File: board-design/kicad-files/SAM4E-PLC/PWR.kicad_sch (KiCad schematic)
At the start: 21 parts, among them Q1 BC817, U14 LM2576HVS-3.3

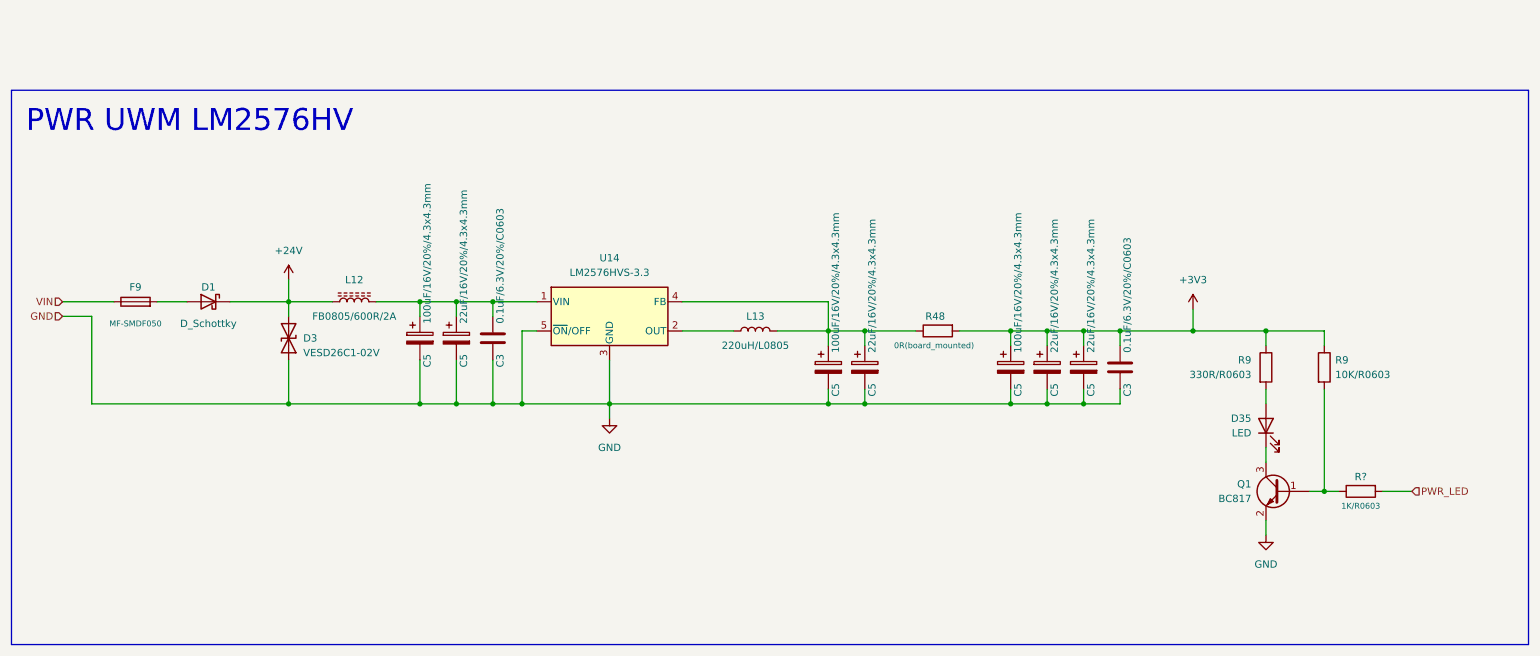
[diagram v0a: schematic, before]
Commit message: [UPDATE]
Refactored schematic for LTE, Power and other schematic sub-sheets.

Signed-off-by: Nicolae-Andrei Vasile <vasilenicolaeandrei@gmail.com>
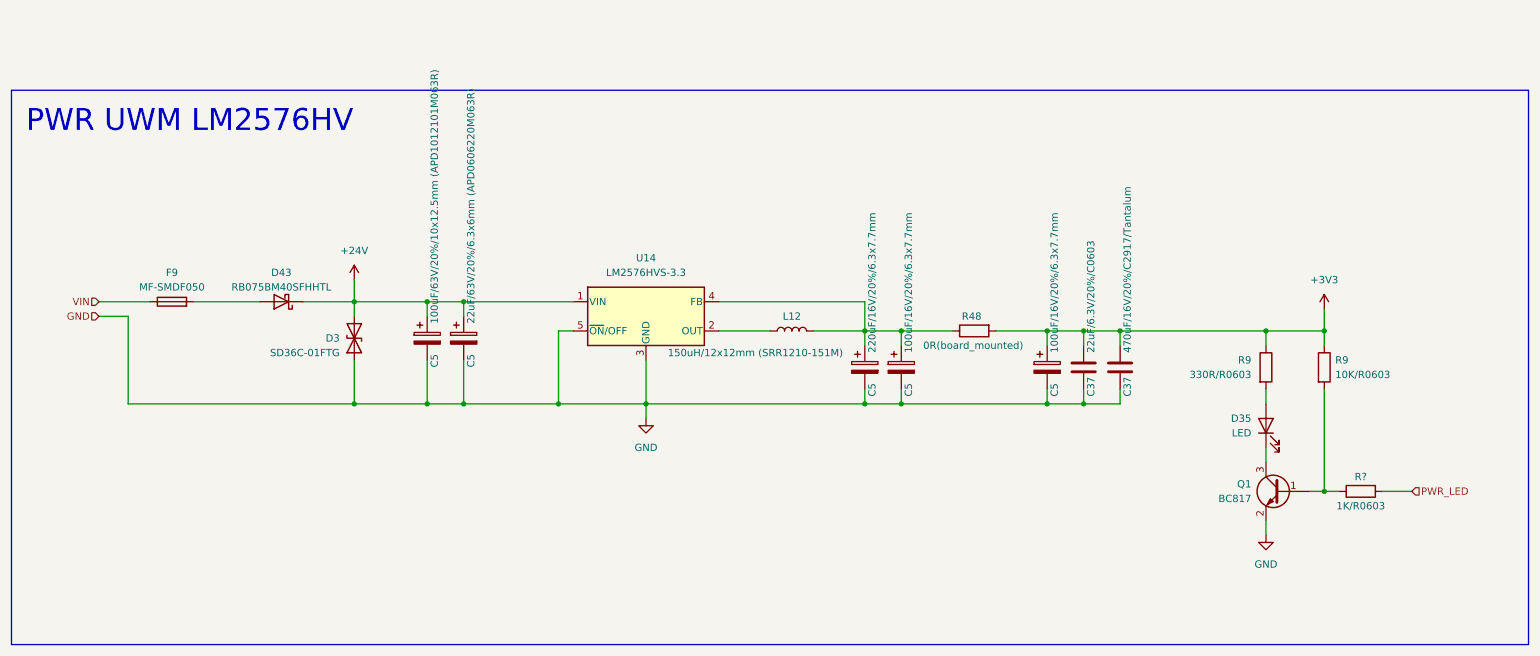
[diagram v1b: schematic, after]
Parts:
- removed C3 (x2): 0.1uF/6.3V/20%/C0603, symbol Device:C
- removed C5 (x2): 22uF/16V/20%/4.3x4.3mm, symbol Device:C_Polarized
- removed C5: 100uF/16V/20%/4.3x4.3mm, symbol Device:C_Polarized
- removed D1: D_Schottky, symbol SparkFun-DiscreteSemi:D_Schottky
- removed L12: FB0805/600R/2A, symbol Device:L_Ferrite
- added C37: 470uF/16V/20%/C2917/Tantalum, Capacitor_Tantalum_SMD:CP_EIA-7343-30_AVX-N, symbol Device:C
- added C37: 22uF/6.3V/20%/C0603, symbol Device:C
- added C5: 100uF/16V/20%/6.3x7.7mm, Capacitor_SMD:CP_Elec_6.3x7.7, symbol Device:C_Polarized
- added D43: RB075BM40SFHHTL, digikey-footprints:TO-252-3, symbol Device:D_Schottky
- C5: value 22uF/16V/20%/4.3x4.3mm -> 22uF/63V/20%/6.3x6mm (APD0606220M063R); footprint (none) -> Capacitor_SMD:CP_Elec_6.3x5.9
- C5: value 100uF/16V/20%/4.3x4.3mm -> 220uF/16V/20%/6.3x7.7mm; footprint (none) -> Capacitor_SMD:CP_Elec_6.3x7.7
- C5: value 100uF/16V/20%/4.3x4.3mm -> 100uF/63V/20%/10x12.5mm (APD1012101M063R); footprint (none) -> Capacitor_SMD:CP_Elec_10x12.5
- C5: value 22uF/16V/20%/4.3x4.3mm -> 100uF/16V/20%/6.3x7.7mm; footprint (none) -> Capacitor_SMD:CP_Elec_6.3x7.7
- D3: value VESD26C1-02V -> SD36C-01FTG; footprint Diode_SMD:D_SOD-523 -> Diode_SMD:D_SOD-323
- D35: footprint (none) -> LED_SMD:LED_0805_2012Metric
- F9: footprint (none) -> Fuse:Fuse_2010_5025Metric
- L12: renamed from L13; value 220uH/L0805 -> 150uH/12x12mm (SRR1210-151M); footprint (none) -> Inductor_SMD:L_12x12mm_H8mm
- R48: footprint (none) -> Resistor_SMD:R_0402_1005Metric
- R9: footprint (none) -> Resistor_SMD:R_0603_1608Metric
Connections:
- net +24V: now also C5.1, C5.1, U14.1 (VIN), D43.1 (K)
- net +3V3: now also C37.1, C37.1, C5.1
- net GND: now also C37.2, C37.2, C5.2
- net at F9.2: now also D43.2 (A)
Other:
- moved on the sheet: C5, D3, F9, L12, R48, U14

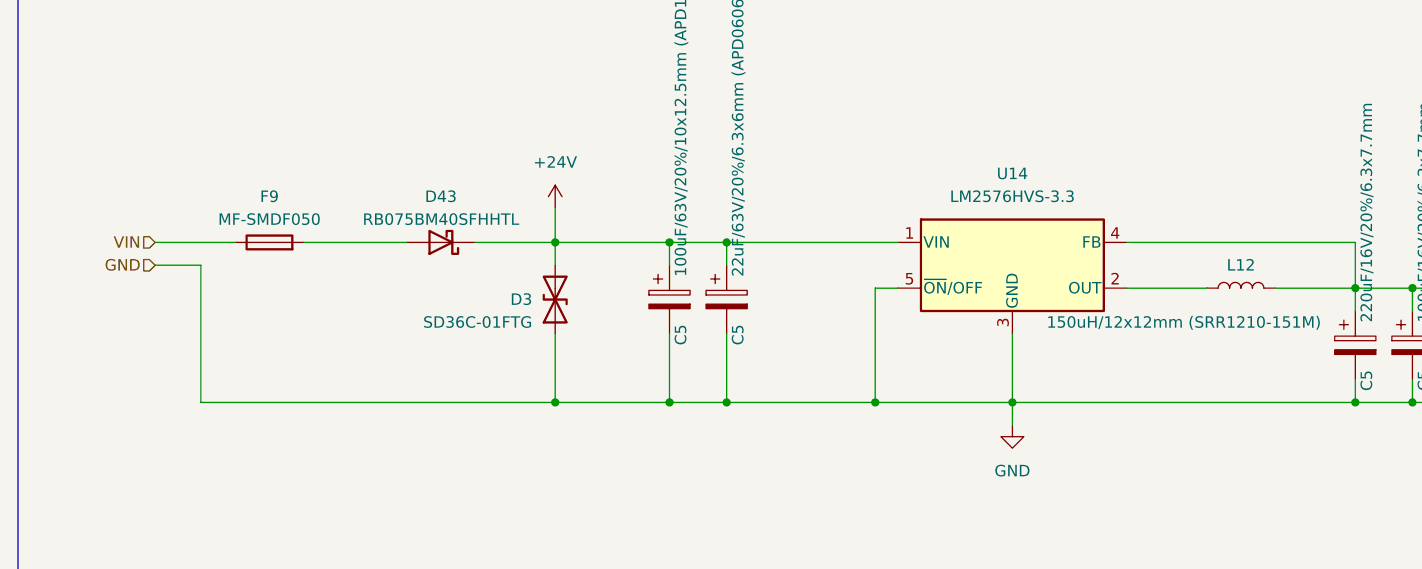
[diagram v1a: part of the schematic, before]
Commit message: [UPDATE]
First draft of SAM4E-PLC schematic completed.

Signed-off-by: Nicolae-Andrei Vasile <vasilenicolaeandrei@gmail.com>
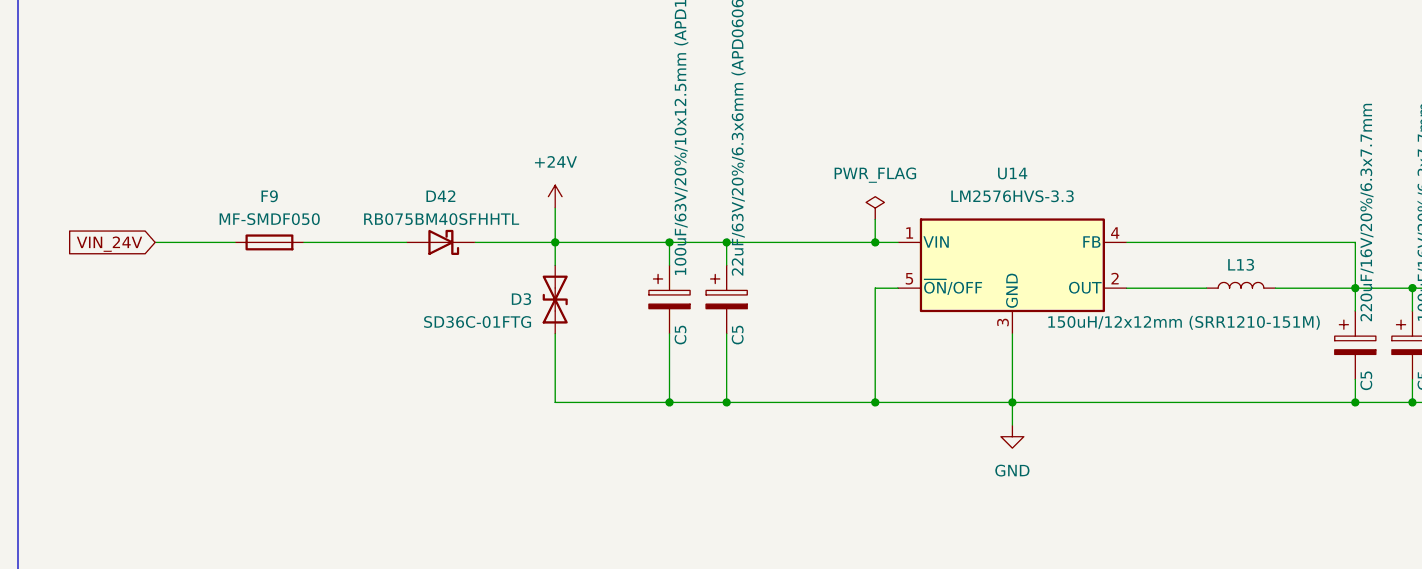
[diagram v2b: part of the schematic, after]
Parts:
- renumbered D43 to D42, L12 to L13
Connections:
- net VIN renamed VIN_24V
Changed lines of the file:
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@@
   (junction (at 196.85 97.79) (diameter 0) (color 0 0 0 0)
   )
+  (junction (at 111.76 92.71) (diameter 0) (color 0 0 0 0)
+  )
   (junction (at 95.25 92.71) (diameter 0) (color 0 0 0 0)
   )
@@
   (junction (at 171.45 110.49) (diameter 0) (color 0 0 0 0)
   )
-  (junction (at 76.2 110.49) (diameter 0) (color 0 0 0 0)
-  )
   (junction (at 95.25 110.49) (diameter 0) (color 0 0 0 0)
   )
@@
     (stroke (width 0) (type default))
   )
-  (wire (pts (xy 36.83 110.49) (xy 76.2 110.49))
-    (stroke (width 0) (type default))
-  )
   (wire (pts (xy 165.1 110.49) (xy 127 110.49))
     (stroke (width 0) (type default))
   )
-  (wire (pts (xy 95.25 92.71) (xy 114.3 92.71))
-    (stroke (width 0) (type default))
-  )
-  (wire (pts (xy 31.75 95.25) (xy 36.83 95.25))
+  (wire (pts (xy 95.25 92.71) (xy 111.76 92.71))
     (stroke (width 0) (type default))
   )
@@
     (stroke (width 0) (type default))
   )
-  (wire (pts (xy 36.83 110.49) (xy 36.83 95.25))
-    (stroke (width 0) (type default))
-  )
   (wire (pts (xy 245.11 125.73) (xy 242.57 125.73))
     (stroke (width 0) (type default))
@@
     (stroke (width 0) (type default))
   )
+  (wire (pts (xy 111.76 90.17) (xy 111.76 92.71))
+    (stroke (width 0) (type default))
+  )
   (wire (pts (xy 88.9 110.49) (xy 95.25 110.49))
     (stroke (width 0) (type default))
@@
   )
   (wire (pts (xy 76.2 92.71) (xy 76.2 95.25))
+    (stroke (width 0) (type default))
+  )
+  (wire (pts (xy 111.76 92.71) (xy 114.3 92.71))
     (stroke (width 0) (type default))
   )
@@
     (effects (font (size 3.81 3.81) (color 140 140 0 1)) (justify left bottom))
   )
+  (global_label "VIN_24V" (shape input) (at 31.75 92.71 180) (fields_autoplaced)
+    (effects (font (size 1.27 1.27)) (justify right))
+    (property "Intersheetrefs" "${INTERSHEET_REFS}" (at 21.2657 92.71 0)
+      (effects (font (size 1.27 1.27)) (justify right) hide)
+    )
+  )
   (hierarchical_label "PWR_LED" (shape input) (at 260.35 125.73 0) (fields_autoplaced)
     (effects (font (size 1.27 1.27)) (justify left))
   )
-  (hierarchical_label "VIN" (shape input) (at 31.75 92.71 180) (fields_autoplaced)
-    (effects (font (size 1.27 1.27)) (justify right))
-  )
-  (hierarchical_label "GND" (shape input) (at 31.75 95.25 180) (fields_autoplaced)
-    (effects (font (size 1.27 1.27)) (justify right))
-  )
   (symbol (lib_id "Device:C_Polarized") (at 196.85 104.14 0) (unit 1)
     (in_bom yes) (on_board yes) (dnp no)
@@
         )
         (path "/93076d8a-73da-4f5d-b7f2-28678f1db77d/aee81a7b-cba1-4b89-a883-459d3f783e91"
-          (reference "C69") (unit 1)
+          (reference "C92") (unit 1)
         )
       )
@@
         )
         (path "/93076d8a-73da-4f5d-b7f2-28678f1db77d/aee81a7b-cba1-4b89-a883-459d3f783e91"
-          (reference "C66") (unit 1)
+          (reference "C89") (unit 1)
         )
       )
@@
         )
         (path "/93076d8a-73da-4f5d-b7f2-28678f1db77d/aee81a7b-cba1-4b89-a883-459d3f783e91"
-          (reference "C71") (unit 1)
+          (reference "C94") (unit 1)
         )
       )
@@
   (symbol (lib_id "power:GND") (at 234.95 133.35 0) (unit 1)
     (in_bom yes) (on_board yes) (dnp no) (fields_autoplaced)
-    (property "Reference" "#PWR072" (at 234.95 139.7 0)
+    (property "Reference" "#PWR085" (at 234.95 139.7 0)
       (effects (font (size 1.27 1.27)) hide)
     )
@@
       (project "SAM4E-PLC"
         (path "/93076d8a-73da-4f5d-b7f2-28678f1db77d/aee81a7b-cba1-4b89-a883-459d3f783e91"
-          (reference "#PWR072") (unit 1)
+          (reference "#PWR085") (unit 1)
         )
       )
@@
   (symbol (lib_id "power:+3V3") (at 245.11 93.98 0) (unit 1)
     (in_bom yes) (on_board yes) (dnp no) (fields_autoplaced)
-    (property "Reference" "#PWR073" (at 245.11 97.79 0)
+    (property "Reference" "#PWR086" (at 245.11 97.79 0)
       (effects (font (size 1.27 1.27)) hide)
     )
@@
       (project "SAM4E-PLC"
         (path "/93076d8a-73da-4f5d-b7f2-28678f1db77d/aee81a7b-cba1-4b89-a883-459d3f783e91"
-          (reference "#PWR073") (unit 1)
+          (reference "#PWR086") (unit 1)
         )
       )
@@
         )
         (path "/93076d8a-73da-4f5d-b7f2-28678f1db77d/aee81a7b-cba1-4b89-a883-459d3f783e91"
-          (reference "C67") (unit 1)
+          (reference "C90") (unit 1)
         )
       )
@@
         )
         (path "/93076d8a-73da-4f5d-b7f2-28678f1db77d/aee81a7b-cba1-4b89-a883-459d3f783e91"
-          (reference "D44") (unit 1)
+          (reference "D43") (unit 1)
         )
       )
@@
   (symbol (lib_id "power:+24V") (at 76.2 88.9 0) (unit 1)
     (in_bom yes) (on_board yes) (dnp no) (fields_autoplaced)
-    (property "Reference" "#PWR070" (at 76.2 92.71 0)
+    (property "Reference" "#PWR083" (at 76.2 92.71 0)
       (effects (font (size 1.27 1.27)) hide)
     )
@@
       (project "SAM4E-PLC"
         (path "/93076d8a-73da-4f5d-b7f2-28678f1db77d/aee81a7b-cba1-4b89-a883-459d3f783e91"
-          (reference "#PWR070") (unit 1)
+          (reference "#PWR083") (unit 1)
         )
       )
@@
   (symbol (lib_id "power:GND") (at 127 113.03 0) (unit 1)
     (in_bom yes) (on_board yes) (dnp no) (fields_autoplaced)
-    (property "Reference" "#PWR071" (at 127 119.38 0)
+    (property "Reference" "#PWR084" (at 127 119.38 0)
       (effects (font (size 1.27 1.27)) hide)
     )
@@
       (project "SAM4E-PLC"
         (path "/93076d8a-73da-4f5d-b7f2-28678f1db77d/aee81a7b-cba1-4b89-a883-459d3f783e91"
-          (reference "#PWR071") (unit 1)
+          (reference "#PWR084") (unit 1)
         )
       )
@@
         )
         (path "/93076d8a-73da-4f5d-b7f2-28678f1db77d/aee81a7b-cba1-4b89-a883-459d3f783e91"
-          (reference "C65") (unit 1)
+          (reference "C88") (unit 1)
         )
       )
@@
         )
         (path "/93076d8a-73da-4f5d-b7f2-28678f1db77d/aee81a7b-cba1-4b89-a883-459d3f783e91"
-          (reference "R113") (unit 1)
+          (reference "R120") (unit 1)
         )
       )
@@
         )
         (path "/93076d8a-73da-4f5d-b7f2-28678f1db77d/aee81a7b-cba1-4b89-a883-459d3f783e91"
-          (reference "R114") (unit 1)
+          (reference "R121") (unit 1)
         )
       )
@@
         )
         (path "/93076d8a-73da-4f5d-b7f2-28678f1db77d/aee81a7b-cba1-4b89-a883-459d3f783e91"
-          (reference "R115") (unit 1)
+          (reference "R122") (unit 1)
         )
       )
@@
         )
         (path "/93076d8a-73da-4f5d-b7f2-28678f1db77d/aee81a7b-cba1-4b89-a883-459d3f783e91"
-          (reference "C70") (unit 1)
+          (reference "C93") (unit 1)
         )
       )
@@
   (symbol (lib_id "Device:L") (at 152.4 97.79 90) (unit 1)
     (in_bom yes) (on_board yes) (dnp no)
-    (property "Reference" "L12" (at 152.4 95.25 90)
+    (property "Reference" "L13" (at 152.4 95.25 90)
       (effects (font (size 1.27 1.27)))
     )
@@
       (project "SAM4E-PLC"
         (path "/93076d8a-73da-4f5d-b7f2-28678f1db77d/aee81a7b-cba1-4b89-a883-459d3f783e91"
-          (reference "L12") (unit 1)
+          (reference "L13") (unit 1)
         )
       )
@@
         )
         (path "/93076d8a-73da-4f5d-b7f2-28678f1db77d/aee81a7b-cba1-4b89-a883-459d3f783e91"
-          (reference "C68") (unit 1)
+          (reference "C91") (unit 1)
         )
       )
@@
         )
         (path "/93076d8a-73da-4f5d-b7f2-28678f1db77d/aee81a7b-cba1-4b89-a883-459d3f783e91"
-          (reference "D45") (unit 1)
+          (reference "D44") (unit 1)
         )
       )
@@
         )
         (path "/93076d8a-73da-4f5d-b7f2-28678f1db77d/aee81a7b-cba1-4b89-a883-459d3f783e91"
-          (reference "R112") (unit 1)
+          (reference "R119") (unit 1)
+        )
+      )
+    )
+  )
+  (symbol (lib_id "power:PWR_FLAG") (at 111.76 90.17 0) (unit 1)
+    (in_bom yes) (on_board yes) (dnp no) (fields_autoplaced)
+    (property "Reference" "#FLG016" (at 111.76 88.265 0)
+      (effects (font (size 1.27 1.27)) hide)
+    )
+    (property "Value" "PWR_FLAG" (at 111.76 85.09 0)
+      (effects (font (size 1.27 1.27)))
+    )
+    (property "Footprint" "" (at 111.76 90.17 0)
+      (effects (font (size 1.27 1.27)) hide)
+    )
+    (property "Datasheet" "~" (at 111.76 90.17 0)
+      (effects (font (size 1.27 1.27)) hide)
+    )
+    (pin "1")
+    (instances
+      (project "SAM4E-PLC"
+        (path "/93076d8a-73da-4f5d-b7f2-28678f1db77d/f76e13f7-6a24-4ea6-98c5-a4d0bd3b3ced"
+          (reference "#FLG016") (unit 1)
+        )
+        (path "/93076d8a-73da-4f5d-b7f2-28678f1db77d/aee81a7b-cba1-4b89-a883-459d3f783e91"
+          (reference "#FLG017") (unit 1)
         )
       )
@@
   (symbol (lib_id "Device:D_Schottky") (at 63.5 92.71 180) (unit 1)
     (in_bom yes) (on_board yes) (dnp no)
-    (property "Reference" "D43" (at 63.5 87.63 0)
+    (property "Reference" "D42" (at 63.5 87.63 0)
       (effects (font (size 1.27 1.27)))
     )
@@
       (project "SAM4E-PLC"
         (path "/93076d8a-73da-4f5d-b7f2-28678f1db77d/aee81a7b-cba1-4b89-a883-459d3f783e91"
-          (reference "D43") (unit 1)
-        )
-      )
+          (reference "D42") (unit 1)
+        )
+      )

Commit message: [IN PROGRESS]
SAM4E-PLC PCB design in progress.

Signed-off-by: Nicolae-Andrei Vasile <vasilenicolaeandrei@gmail.com>
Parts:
- C37: footprint (none) -> Capacitor_SMD:C_0603_1608Metric
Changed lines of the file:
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@@
       (effects (font (size 1.27 1.27)) (justify left))
     )
-    (property "Footprint" "" (at 204.1652 107.95 0)
+    (property "Footprint" "Capacitor_SMD:C_0603_1608Metric" (at 204.1652 107.95 0)
       (effects (font (size 1.27 1.27)) hide)
     )

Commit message: [UPDATE]
Work in progress.

Signed-off-by: Nicolae-Andrei Vasile <vasilenicolaeandrei@gmail.com>
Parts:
- D35: renamed from D42; value RB075BM40SFHHTL -> RB088LAM-40TFTR; footprint digikey-footprints:TO-252-3 -> Diode_SMD:D_SOD-128
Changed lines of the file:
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@@
         )
         (path "/93076d8a-73da-4f5d-b7f2-28678f1db77d/aee81a7b-cba1-4b89-a883-459d3f783e91"
-          (reference "D43") (unit 1)
+          (reference "D36") (unit 1)
         )
       )
@@
         )
         (path "/93076d8a-73da-4f5d-b7f2-28678f1db77d/aee81a7b-cba1-4b89-a883-459d3f783e91"
-          (reference "R120") (unit 1)
+          (reference "R112") (unit 1)
         )
       )
@@
         )
         (path "/93076d8a-73da-4f5d-b7f2-28678f1db77d/aee81a7b-cba1-4b89-a883-459d3f783e91"
-          (reference "R121") (unit 1)
+          (reference "R113") (unit 1)
         )
       )
@@
         )
         (path "/93076d8a-73da-4f5d-b7f2-28678f1db77d/aee81a7b-cba1-4b89-a883-459d3f783e91"
-          (reference "R122") (unit 1)
+          (reference "R114") (unit 1)
         )
       )
@@
         )
         (path "/93076d8a-73da-4f5d-b7f2-28678f1db77d/aee81a7b-cba1-4b89-a883-459d3f783e91"
-          (reference "D44") (unit 1)
+          (reference "D37") (unit 1)
         )
       )
@@
         )
         (path "/93076d8a-73da-4f5d-b7f2-28678f1db77d/aee81a7b-cba1-4b89-a883-459d3f783e91"
-          (reference "R119") (unit 1)
+          (reference "R111") (unit 1)
         )
       )
@@
   (symbol (lib_id "Device:D_Schottky") (at 63.5 92.71 180) (unit 1)
     (in_bom yes) (on_board yes) (dnp no)
-    (property "Reference" "D42" (at 63.5 87.63 0)
-      (effects (font (size 1.27 1.27)))
-    )
-    (property "Value" "RB075BM40SFHHTL" (at 63.5 90.17 0)
-      (effects (font (size 1.27 1.27)))
-    )
-    (property "Footprint" "digikey-footprints:TO-252-3" (at 63.5 92.71 0)
-      (effects (font (size 1.27 1.27)) hide)
-    )
-    (property "Datasheet" "https://fscdn.rohm.com/en/products/databook/datasheet/discrete/diode/schottky_barrier/rb075bm40sfhhtl-e.pdf" (at 63.5 92.71 0)
-      (effects (font (size 1.27 1.27)) hide)
-    )
-    (pin "1")
-    (pin "2")
-    (instances
-      (project "SAM4E-PLC"
-        (path "/93076d8a-73da-4f5d-b7f2-28678f1db77d/aee81a7b-cba1-4b89-a883-459d3f783e91"
-          (reference "D42") (unit 1)
-        )
-      )
+    (property "Reference" "D35" (at 63.5 87.63 0)
+      (effects (font (size 1.27 1.27)))
+    )
+    (property "Value" "RB088LAM-40TFTR" (at 63.5 90.17 0)
+      (effects (font (size 1.27 1.27)))
+    )
+    (property "Footprint" "Diode_SMD:D_SOD-128" (at 63.5 92.71 0)
+      (effects (font (size 1.27 1.27)) hide)
+    )
+    (property "Datasheet" "https://fscdn.rohm.com/en/products/databook/datasheet/discrete/diode/schottky_barrier/rb088lam-40tftr-e.pdf" (at 63.5 92.71 0)
+      (effects (font (size 1.27 1.27)) hide)
+    )
+    (pin "1")
+    (pin "2")
+    (instances
+      (project "SAM4E-PLC"
+        (path "/93076d8a-73da-4f5d-b7f2-28678f1db77d/aee81a7b-cba1-4b89-a883-459d3f783e91"
+          (reference "D35") (unit 1)
+        )
+      )
